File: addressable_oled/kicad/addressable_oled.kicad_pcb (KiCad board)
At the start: 2 copper layers, 35.6 x 35.6 mm, 21 parts, among them J1 Conn_01x05_Pin, J2 Conn_01x03_Socket, U1 SLG46826G, U2 OLED-128O064D

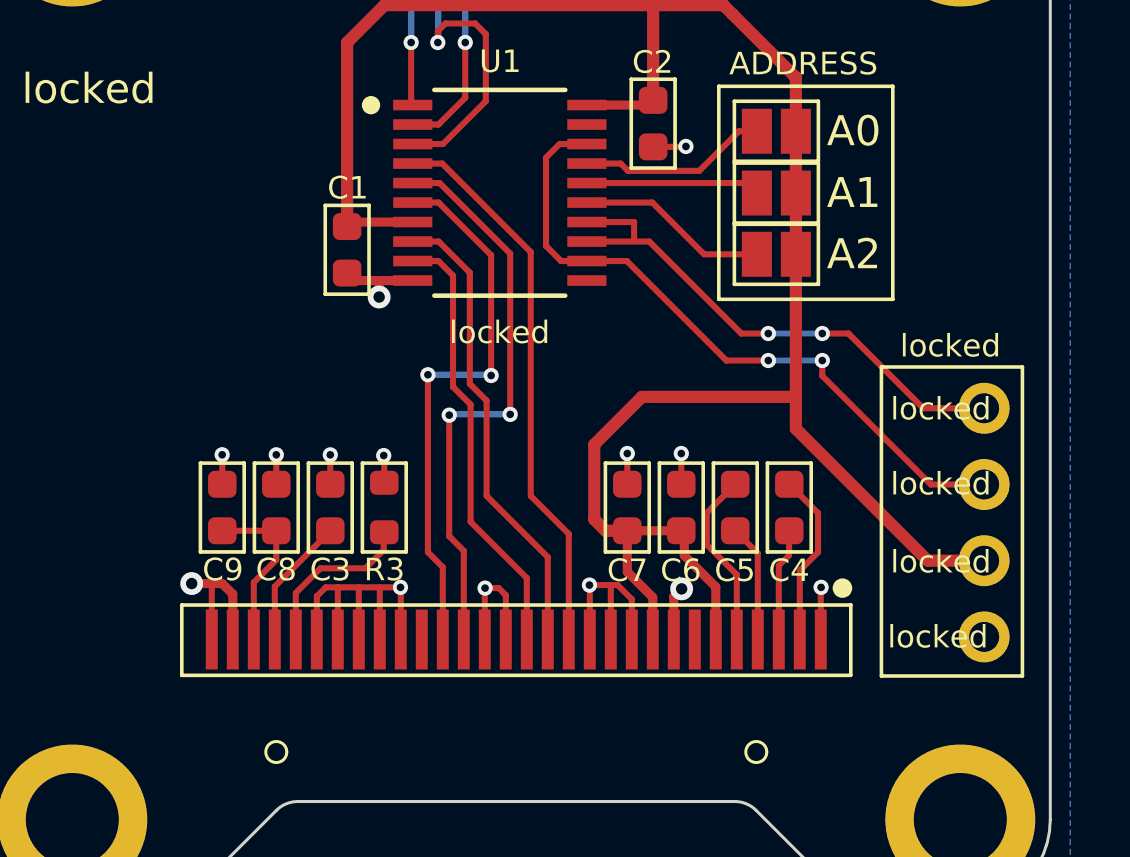
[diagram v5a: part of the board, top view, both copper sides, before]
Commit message: Extended display pad from 2mm to 3mm.
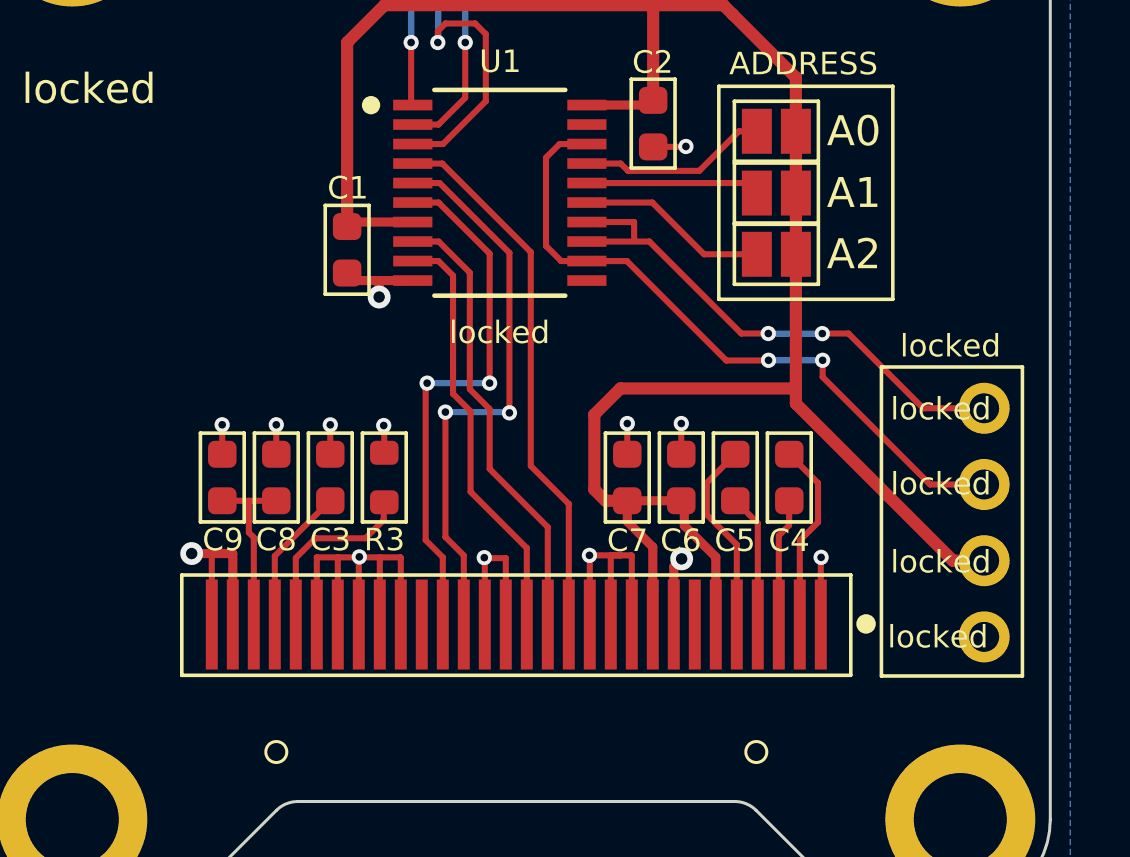
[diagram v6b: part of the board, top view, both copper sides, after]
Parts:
- moved C3 1.00 mm to (-6.20, 3.40)
- moved C4 1.00 mm to (9.10, 3.40)
- moved C5 1.00 mm to (7.30, 3.40)
- moved C6 1.00 mm to (5.50, 3.40)
- moved C7 1.00 mm to (3.70, 3.40)
- moved C8 1.00 mm to (-8.00, 3.40)
- moved C9 1.00 mm to (-9.80, 3.40)
- moved R3 1.00 mm to (-4.40, 3.40)
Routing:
- net GND: track 40.7 -> 41.8 mm
- net /OLED_MOSI: track 18.5 -> 17.5 mm
- net /OLED_DC: track 14.7 -> 13.7 mm
- net /OLED_RST: track 15.6 -> 14.6 mm
- net /OLED_CS: track 18.6 -> 17.6 mm
- net VDD: track 74.3 -> 73.4 mm
- net /OLED_CLK: track 19.3 -> 18.5 mm

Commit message: Final cleanup.
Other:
- board text added: "GND"
- board text added: "PROG"
- board text added: "RECOMANDED 1mm PCB"
- board text added: "SCL"
- board text added: "SDA"
- board text added: "VCC"
